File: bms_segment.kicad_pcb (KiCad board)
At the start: 4 copper layers, 120 x 65 mm, 204 parts, among them J1 Conn_02x17_Counter_Clockwise, J2 Conn_02x10_Odd_Even, J3 Conn_02x10_Odd_Even, J4 Conn_01x04, J5 Conn_01x04, J7 Conn_01x06, Q1 IRLML0060, Q10 IRLML0060, Q11 IRLML0060, Q12 IRLML0060, Q13 IRLML0060, Q14 IRLML0060, Q15 IRLML0060, Q16 IRLML0060, Q17 BSS84, Q2 IRLML0060, Q3 IRLML0060, Q4 IRLML0060, Q5 IRLML0060, Q6 IRLML0060, Q7 IRLML0060, Q8 IRLML0060, Q9 IRLML0060, SW1 SW_Push, U1 LMR516xx, U2 MAX14921, U3 MAX11163, U4 REF61xx, U5 STM32F103C8Tx, U6 ADuM1252, U7 74LV4051A, U8 74LV4051A, U9 74LV4051A

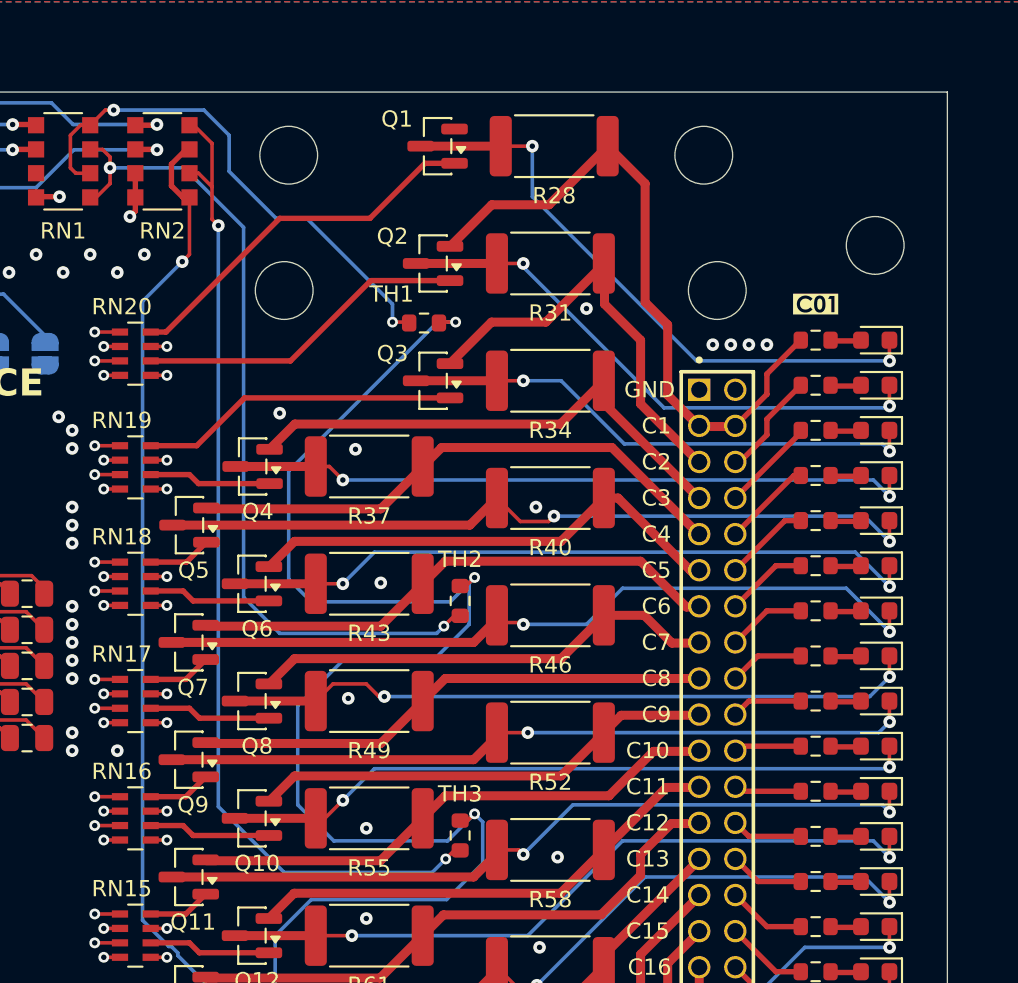
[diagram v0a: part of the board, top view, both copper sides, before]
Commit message: Added keystone test point for GND
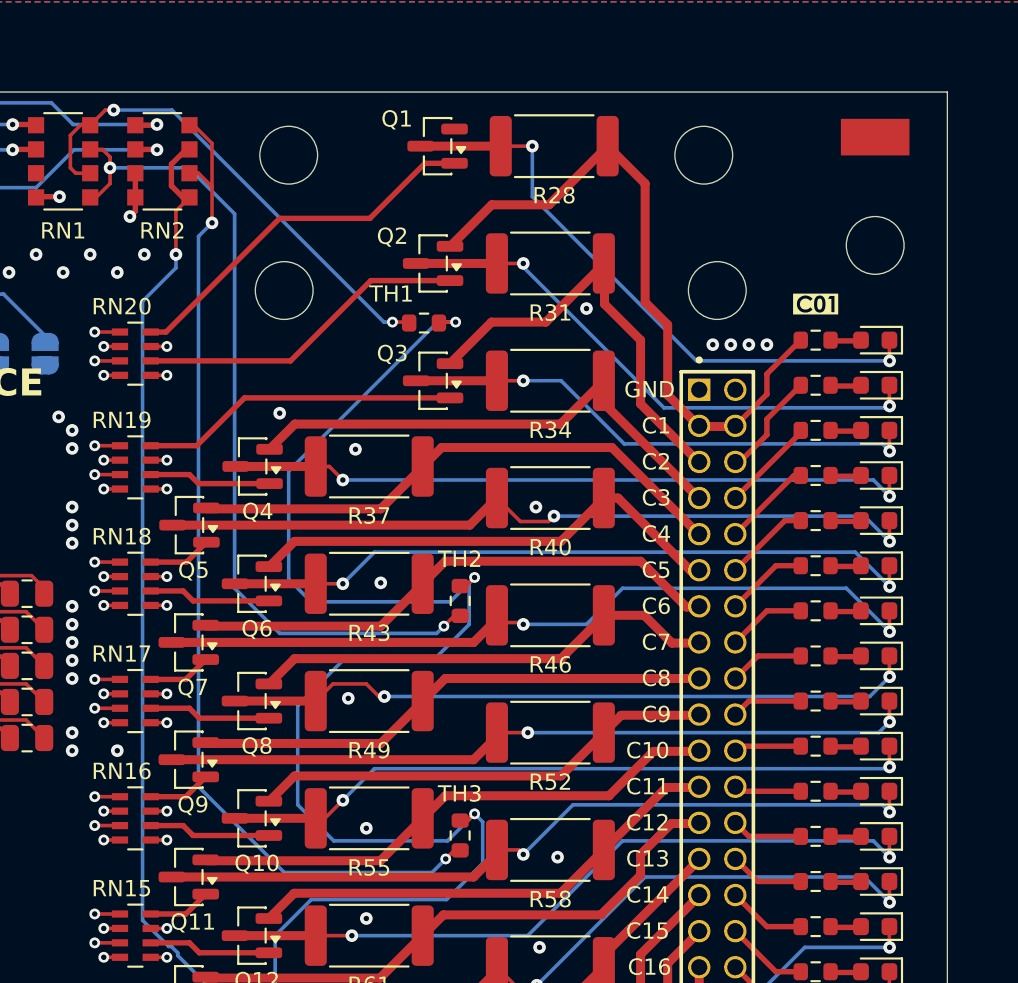
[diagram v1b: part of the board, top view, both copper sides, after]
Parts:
- added TP6: GND, yfs:KEYSTONE_5019, F.Cu at (215.0, 53.5)
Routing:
- net /Thermistor Sampling/Thermistors/Network/IN_1: track 29.0 -> 27.2 mm
- net /Thermistor Sampling/Thermistors/Network1/IN_1: track 54.9 -> 55.5 mm

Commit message: *: Final cleanup for revision E
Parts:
- added kibuzzard-69EF73A7: G***, kibuzzard-69EF73A7, F.Cu at (215.0, 55.7)
- TP6: value GND -> TestPoint; footprint yfs:KEYSTONE_5019 -> TestPoint:TestPoint_Keystone_5019_Miniature

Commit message: *: Rework BOM
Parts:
- RN1, RN10, RN11, RN12, RN2, RN3, RN4, RN5, RN6, RN7, RN8, RN9: value 1k -> 10k
- renumbered J7 to J6
